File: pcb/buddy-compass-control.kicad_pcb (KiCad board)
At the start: 2 copper layers, 50.8 x 50.8 mm, 46 parts, among them J1 USB_C_Receptacle_USB2.0, J2 Conn_01x02, J3 Conn_ARM_JTAG_SWD_10, J4 Conn_02x05_Odd_Even, Q1 DMG2301L, SW1 SW_Push, SW2 SW_Push, SW3 SW_Push, SW4 SW_Push, SW5 SW_Push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

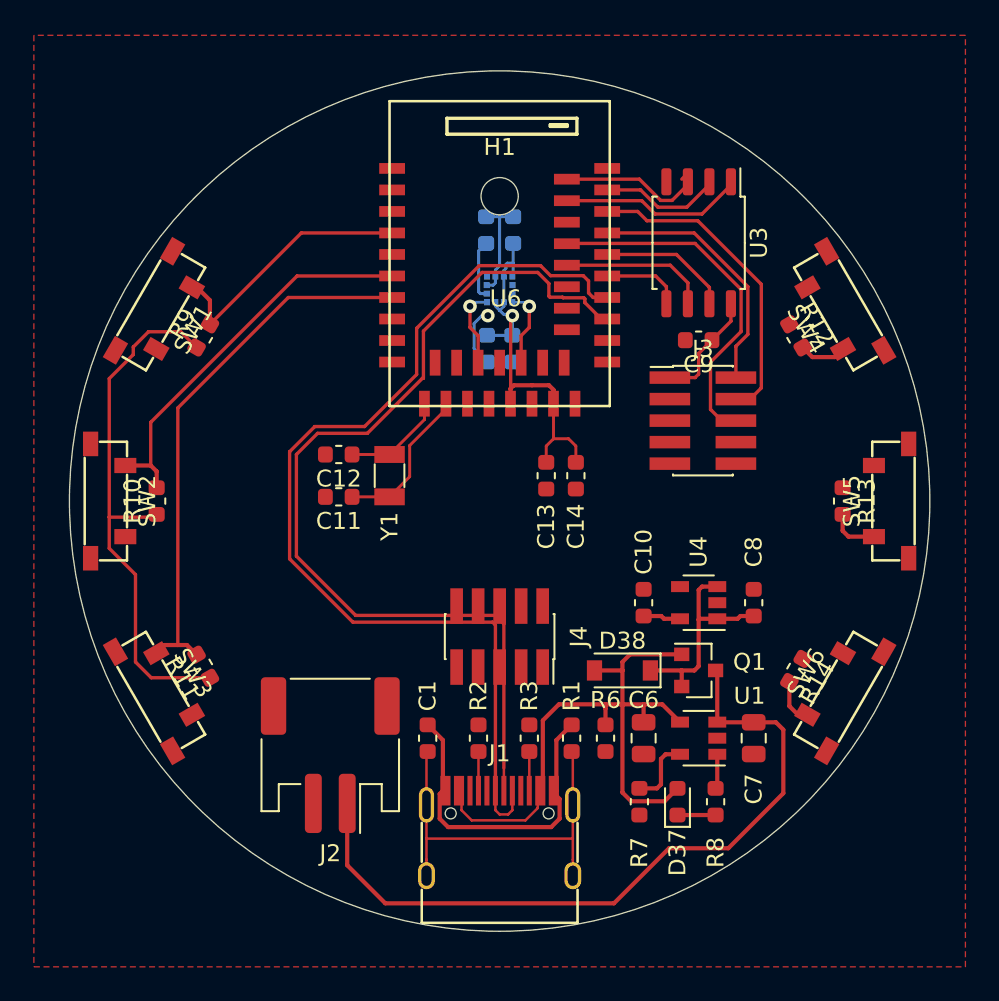
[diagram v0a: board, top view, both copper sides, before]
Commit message: Control board routing finished.
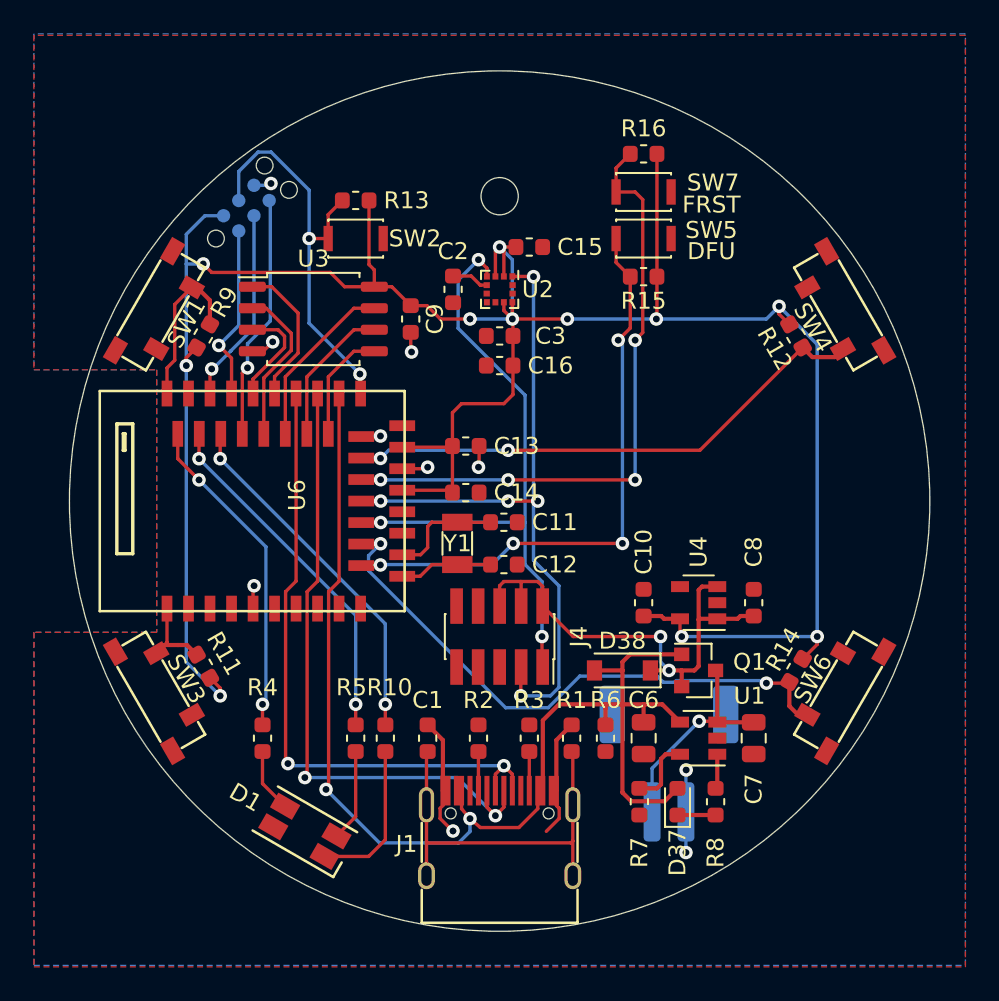
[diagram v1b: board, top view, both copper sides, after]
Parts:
- added D1: LED_RGBC, LED_SMD:LED_RGB_1210, F.Cu at (38.5, 69.5)
- added R15: 47K, Resistor_SMD:R_0603_1608Metric, F.Cu at (58.5, 36.8)
- added R16: 47K, Resistor_SMD:R_0603_1608Metric, F.Cu at (58.5, 29.5)
- added R4: 220, Resistor_SMD:R_0603_1608Metric, F.Cu at (36.0, 64.0)
- added R5: 220, Resistor_SMD:R_0603_1608Metric, F.Cu at (41.5, 64.0)
- added SW7: SW_Push, Button_Switch_SMD:SW_SPST_CK_KXT3, F.Cu at (58.5, 31.8)
- C15, C16, C2, C3, U2: moved to F.Cu
- J2: moved to B.Cu
- J3: value Conn_ARM_JTAG_SWD_10 -> Conn_02x03_Odd_Even; footprint Connector_PinHeader_1.27mm:PinHeader_2x05_P1.27mm_Vertical_SMD -> Connector:Tag-Connect_TC2030-IDC-NL_2x03_P1.27mm_Vertical; moved to B.Cu
- R10: value 47K -> 220
- SW2, SW5: footprint buddy-compass-parts:TS-1236VW -> Button_Switch_SMD:SW_SPST_CK_KXT3
- moved R13 33.8 mm to (41.5, 32.2), turned to 180 degrees
- moved J3 29.7 mm to (35.0, 32.7), turned to 45 degrees
- moved U3 23.2 mm to (39.0, 39.2), turned to 0 degrees
- moved SW2 21.2 mm to (41.5, 34.5), turned to 0 degrees
- moved SW5 21.2 mm to (58.5, 34.5), turned to 0 degrees
- moved U6 20.5 mm to (35.5, 50.0), turned to 90 degrees
- moved J2 20.0 mm to (60.0, 65.5), turned to 0 degrees
- moved R10 19.4 mm to (43.2, 64.0), turned to 270 degrees
- moved C9 17.0 mm to (44.8, 39.2), turned to 270 degrees
- moved C12 11.7 mm to (50.2, 53.8), turned to 0 degrees
- moved C11 9.86 mm to (50.2, 51.2), turned to 0 degrees
- moved C14 6.58 mm to (48.0, 49.5), turned to 0 degrees
- moved Y1 5.66 mm to (47.5, 52.5), turned to 270 degrees
- moved C13 5.06 mm to (48.0, 46.8), turned to 0 degrees
- moved C2 4.01 mm to (47.2, 37.5), turned to 270 degrees
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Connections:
- J3 pad 3: GND -> /RESET
- R10 pad 1: +3V3 -> /STATUS_R
- R10 pad 2: /BUTTON2 -> Net-(D1-Pad1)
- R13 pad 2: /BUTTON5 -> /RESET
- SW2 pad 1: /BUTTON2 -> /RESET
- SW5 pad 1: /BUTTON5 -> /DFU
- U6 pad 1: (no net) -> /BUTTON3
- U6 pad 12: (no net) -> /DFU
- U6 pad 14: (no net) -> /BUTTON6
- U6 pad 18: (no net) -> /SCL
- U6 pad 20: /SCL -> /FRST
- U6 pad 22: /BUTTON6 -> /BUTTON4
- U6 pad 28: /BUTTON5 -> /QSPI_D0
- U6 pad 30: (no net) -> /QSPI_SCK
- U6 pad 32: (no net) -> /QSPI_D3
- U6 pad 33: /QSPI_D0 -> /QSPI_CS
- U6 pad 34: /QSPI_SCK -> /QSPI_D1
- U6 pad 35: /QSPI_D3 -> /QSPI_D2
- U6 pad 38: (no net) -> /STATUS_R
- U6 pad 4: /BUTTON1 -> (no net)
- U6 pad 40: /QSPI_CS -> /STATUS_G
- U6 pad 41: /QSPI_D1 -> (no net)
- U6 pad 42: /QSPI_D2 -> /STATUS_B
- U6 pad 43: /BUTTON4 -> /BUTTON1
- U6 pad 6: /BUTTON2 -> (no net)
- U6 pad 7: /BUTTON3 -> (no net)
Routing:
- net +3V3: track 66.1 -> 150.4 mm, vias 1 -> 11
- net /FRST: track 0.00 -> 37.3 mm, vias 0 -> 4
- net /SCL: track 4.95 -> 41.0 mm, vias 1 -> 5
- net VBUS: track 40.2 -> 75.1 mm, vias 0 -> 2
- net /DFU: track 0.00 -> 34.7 mm, vias 0 -> 4
- net /SDA: track 4.75 -> 37.5 mm, vias 1 -> 3
- net /BUTTON6: track 2.70 -> 35.0 mm, vias 0 -> 2
- net Net-(C7-Pad1): track 44.0 -> 12.8 mm, vias 0 -> 1
- net /BUTTON4: track 2.81 -> 31.6 mm, vias 0 -> 2
- net /BUTTON3: track 32.2 -> 5.70 mm
- net /RESET: track 0.00 -> 24.3 mm, vias 0 -> 2
- net /BUTTON2: track 23.3 -> 0.00 mm
- net /STATUS_R: track 0.00 -> 21.2 mm, vias 0 -> 2
- net /D+: track 59.5 -> 38.3 mm, vias 0 -> 2
- net /STATUS_G: track 0.00 -> 21.0 mm, vias 0 -> 2
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- added copper zone on B.Cu, net GND
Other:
- board text added: "DFU"
- board text added: "FRST"

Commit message: Added Atmel crypto chip. Renumbered some diodes. Added extra pins on display connector to allow display blanking and future upgrades.
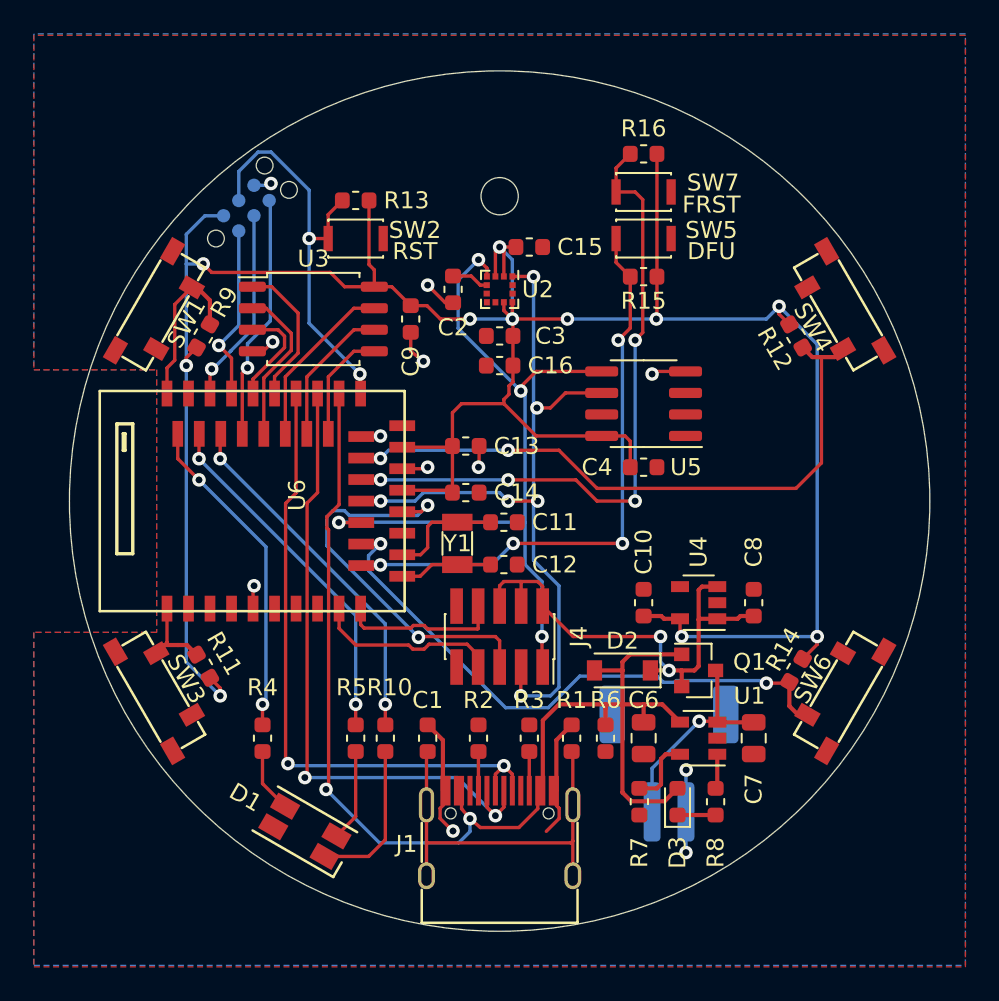
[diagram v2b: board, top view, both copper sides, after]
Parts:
- added C4: 100n, Capacitor_SMD:C_0603_1608Metric, F.Cu at (58.5, 48.0)
- added U5: ATECC608A-SSHDA, Package_SO:SOIC-8_3.9x4.9mm_P1.27mm, F.Cu at (58.5, 44.2)
- renumbered D38 to D2, D37 to D3
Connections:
- J4 pad 5: (no net) -> /SDB
- J4 pad 7: (no net) -> /DISPLAY_IO1
- J4 pad 8: (no net) -> /DISPLAY_IO2
- U6 pad 10: (no net) -> /DISPLAY_IO2
- U6 pad 17: (no net) -> /SDB
- U6 pad 9: (no net) -> /DISPLAY_IO1
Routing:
- net /SDB: track 0.00 -> 23.9 mm, vias 0 -> 2
- net /DISPLAY_IO1: track 0.00 -> 11.0 mm
- net +3V3: track 150.4 -> 160.3 mm
- net /DISPLAY_IO2: track 0.00 -> 9.45 mm
- net /SDA: track 37.5 -> 45.5 mm, vias 3 -> 4
- net /BUTTON4: track 31.6 -> 38.0 mm
- net GND: track 28.6 -> 33.5 mm, vias 10 -> 12
- net /SCL: track 41.0 -> 45.8 mm, vias 5 -> 6
- net /FRST: track 37.3 -> 39.0 mm
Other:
- board text added: "RST"
